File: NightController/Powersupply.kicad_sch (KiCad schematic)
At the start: 0 parts

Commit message: Working on schematic
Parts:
- added C601, C602, C605, C606, C607, C608, C609, C610, C612, C613: 10uF 50V, symbol Device:C
- added C603, C604, C611, C614: 220nF 50V, symbol Device:C
- added D601, D602: LED, symbol Device:LED
- added IC601: BQ24192IRGER, Package_DFN_QFN:VQFN-24-1EP_4x4mm_P0.5mm_EP2.45x2.45mm_ThermalVias, symbol BQ24192I:BQ24192I
- added L601: 2.2uH, symbol Device:L
- added R601, R602, R603, R604: 56k 5%, symbol Device:R
- added R605: 100R 5%, symbol Device:R
- added R606, R609, R610, R611, R612, R613, R614: 100k 5%, symbol Device:R
- added R607, R608: 2.2k 5%, symbol Device:R
- added U601: TLV76733QWDRBxQ1, Package_SON:VSON-8-1EP_3x3mm_P0.65mm_EP1.65x2.4mm, symbol Regulator_Linear:TLV76733QWDRBxQ1
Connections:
- new net: D602.1 (K), R608.1
- new net: C604.1, IC601.21 (BTST)
- new net: C604.2, IC601.19 (SW), IC601.20 (SW), L601.1
- new net: C610.1, IC601.22 (REGN), R603.1
- new net: IC601.11 (TS1), IC601.12 (TS2), R603.2, R604.1
- new net: D601.1 (K), R607.1
- new net: IC601.10 (ILIM), R605.1
- new net +3.3V: C613.1, C614.1, R609.1, R610.1, R611.1, U601.1 (OUT), U601.3 (SNS)
- new net +VSYS: C605.1, C606.1, C607.1, C608.1, C612.1, D601.2 (A), D602.2 (A), IC601.15 (SYS), IC601.16 (SYS), L601.2, U601.5 (EN), U601.8 (IN)
- new net BAT_BAT: C609.1, IC601.13 (BAT), IC601.14 (BAT), R601.1
- new net BAT_INT: IC601.7 (INT), R611.2
- new net BAT_NCE: IC601.9 (~{CE}), R606.1
- new net BAT_NPG: IC601.3 (~{PG}), R607.2
- new net BAT_OTG: IC601.8 (OTG), R612.2
- new net BAT_PMID: C602.1, IC601.23 (PMID)
- new net BAT_PSEL: IC601.2 (PSEL), R613.2
- new net BAT_SCL: IC601.5 (SCL), R609.2
- new net BAT_SDA: IC601.6 (SDA), R610.2
- new net BAT_SNS: C611.1, R601.2, R602.1
- new net BAT_STAT: IC601.4 (STAT), R608.2
- new net GND: C601.2, C602.2, C603.2, C605.2, C606.2, C607.2, C608.2, C609.2, C610.2, C611.2, C612.2, C613.2, C614.2, IC601.17 (PGND), IC601.18 (PGND), IC601.25 (EP), R602.2, R604.2, R605.2, R606.2, R614.1, U601.4 (GND), U601.6 (GND), U601.9 (PAD)
- new net VBUS: C601.1, C603.1, IC601.1 (VBUS), IC601.24 (VBUS), R612.1, R613.1, R614.2
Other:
- note added: "+3.3VDC Supply for MCU and Peripherals"
- note added: "Gain = 0.641"
- note added: "ILIM is set via register"
- note added: "Place battery connector here!"
- note added: "To MCU"
- note added: "To connector"
- note added: "USB and Battery Supply in one chip for 3.3V Regulator and leds"

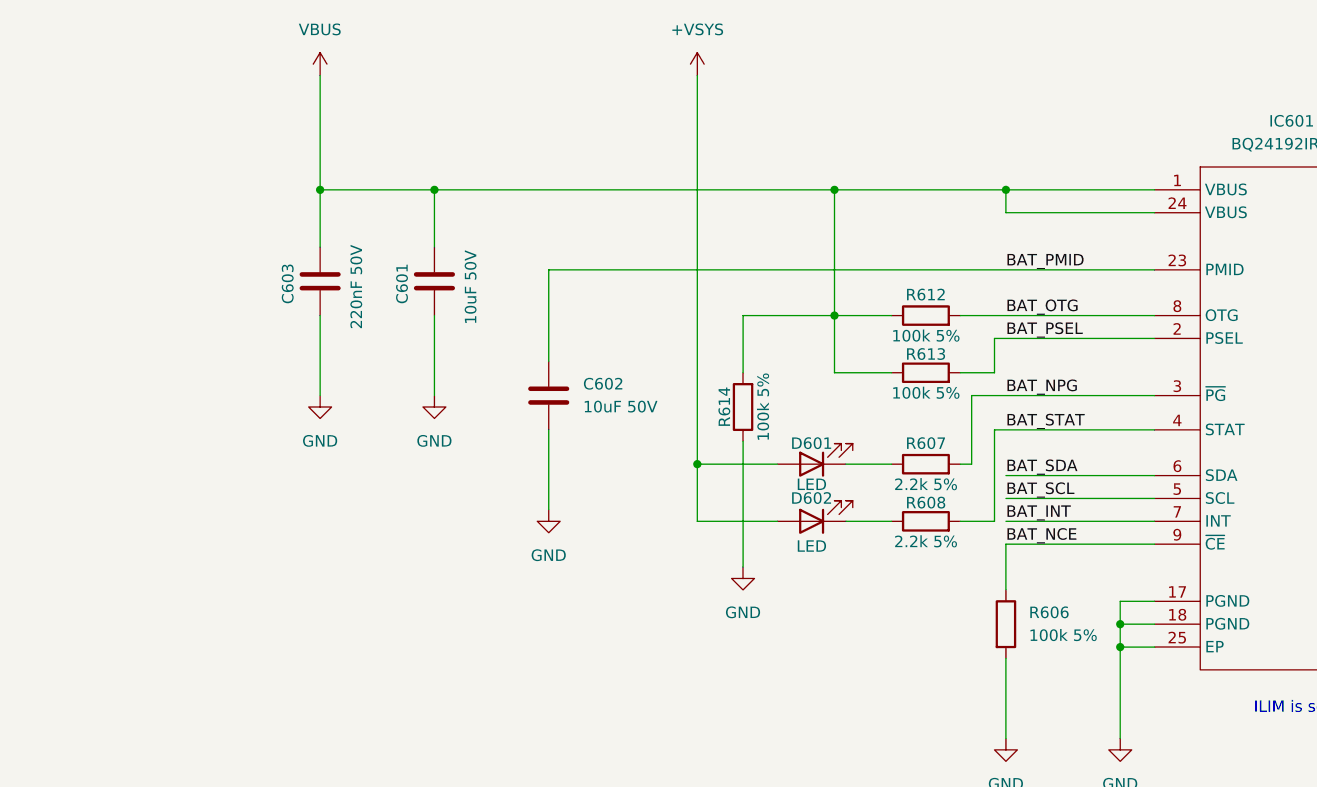
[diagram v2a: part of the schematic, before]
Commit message: update schematic
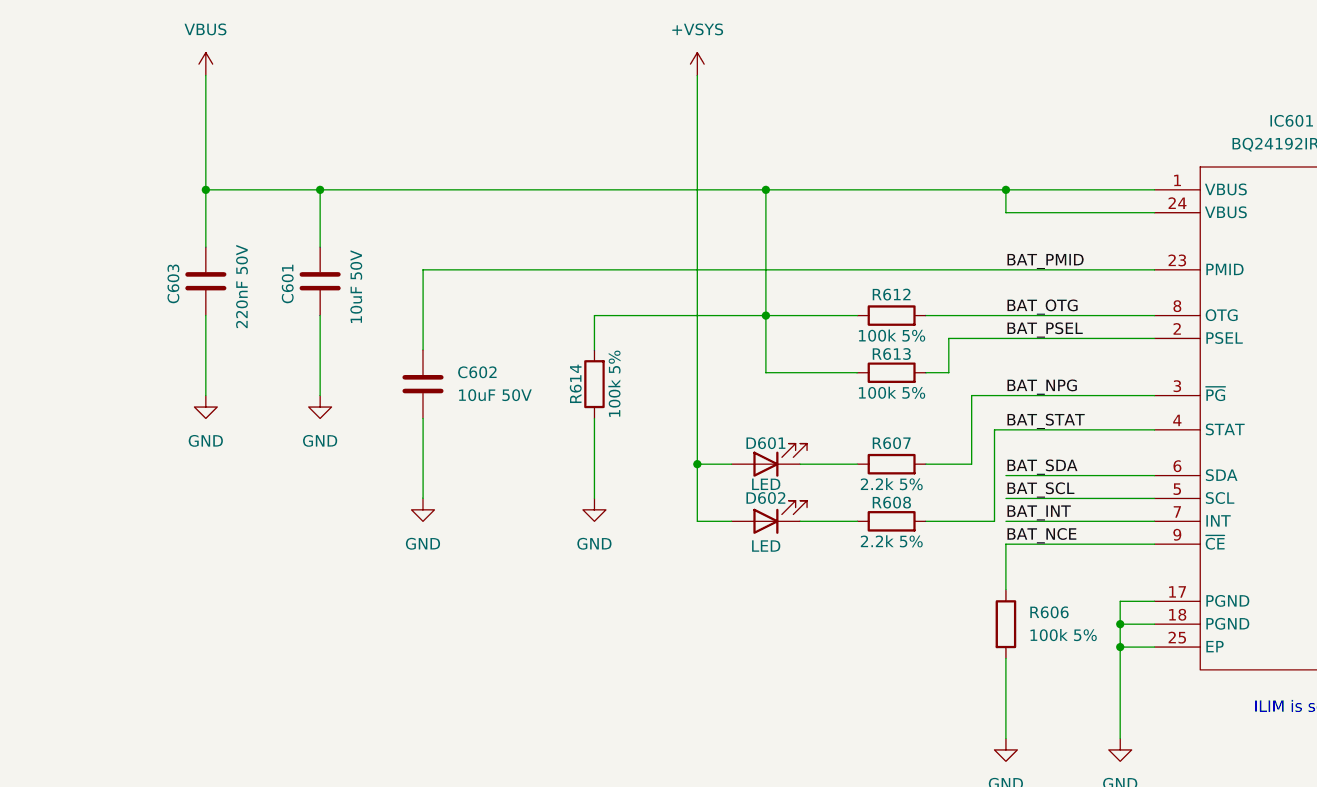
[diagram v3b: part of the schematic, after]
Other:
- moved on the sheet: C601, C602, C603, D601, D602, R607, R608, R612, R613, R614
